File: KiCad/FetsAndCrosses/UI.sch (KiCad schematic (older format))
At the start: 0 parts

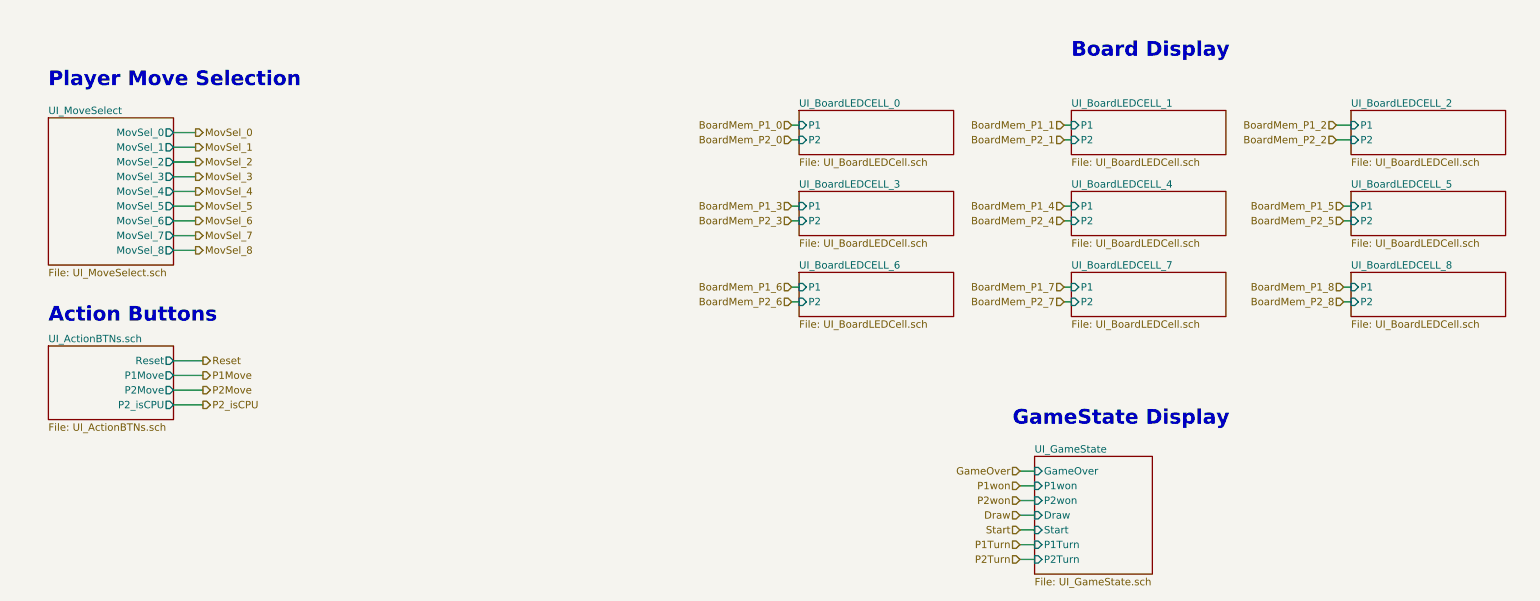
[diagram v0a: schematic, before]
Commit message: Reworked everything to use Buses
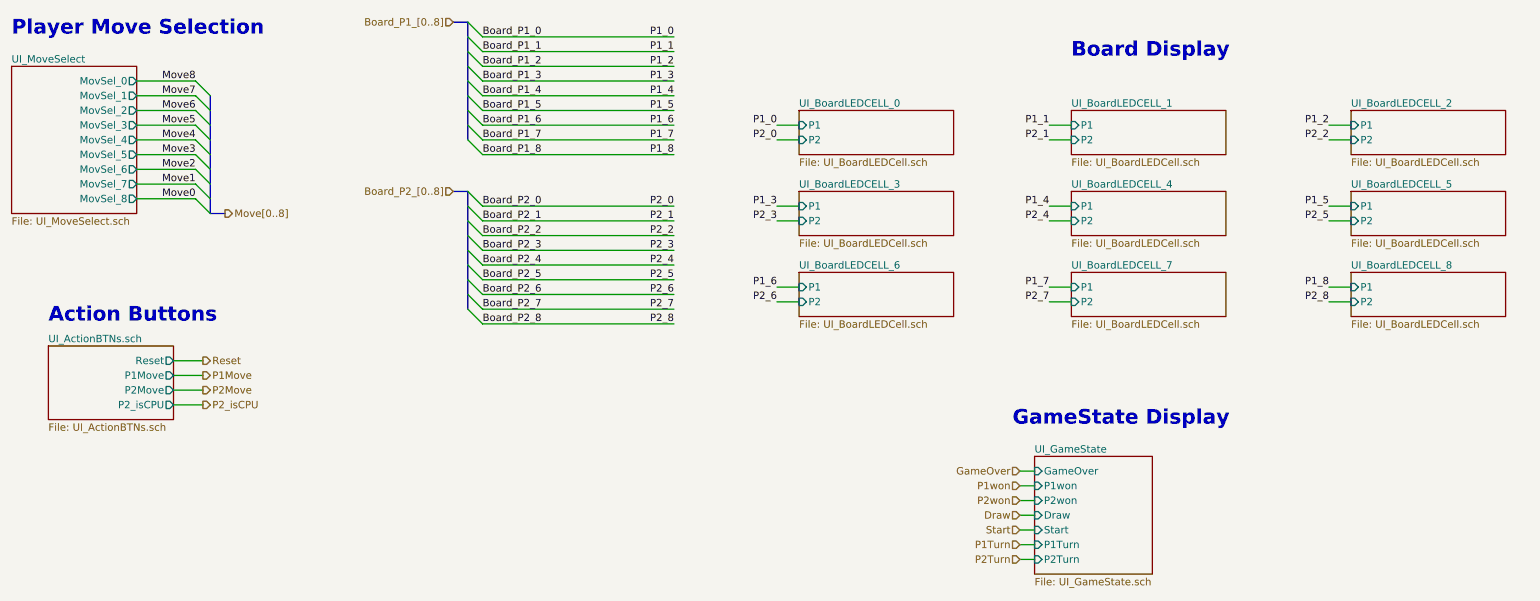
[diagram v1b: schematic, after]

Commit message: Schematic Done, Footprints assigned, ERC OK.
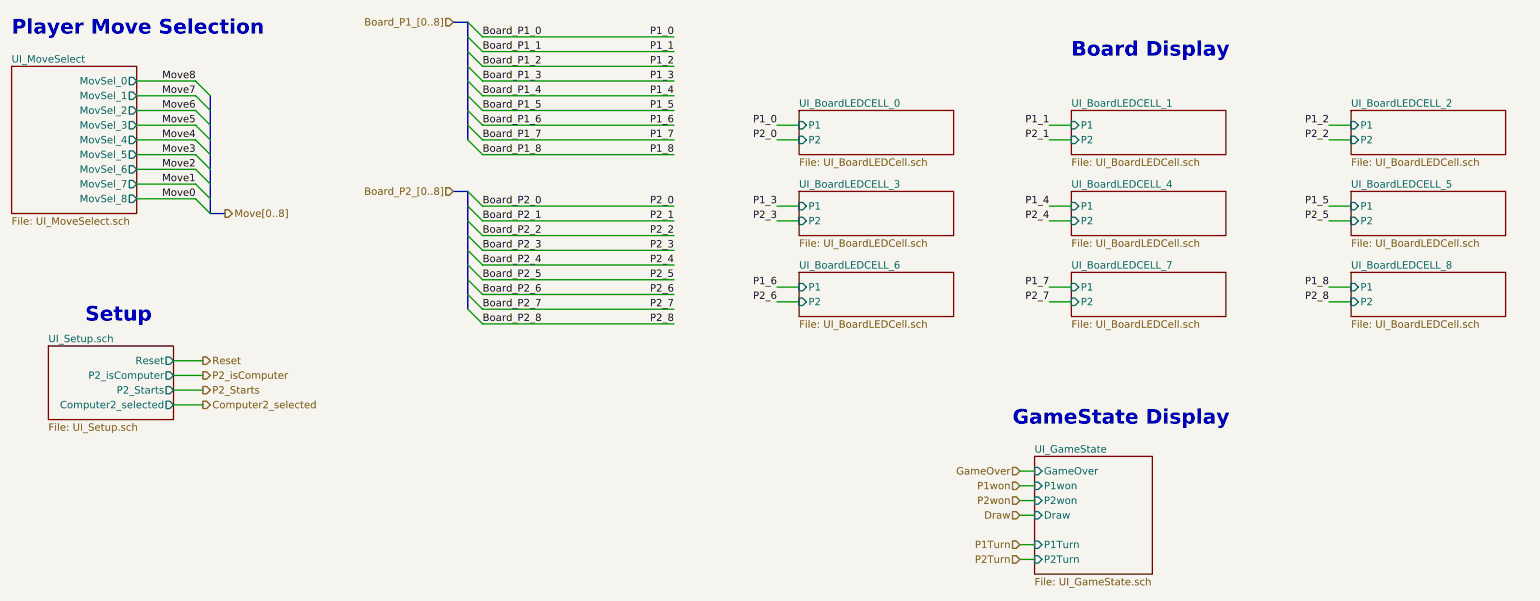
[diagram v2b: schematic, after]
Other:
- note added: "Setup"
- note removed: "Action Buttons"
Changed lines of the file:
@@
 $Descr A4 11693 8268
 encoding utf-8
-Sheet 373 400
+Sheet 373 389
 Title "Fets and Crosses"
 Date ""
@@
 F3 "P2" I L 9800 2850 50
 $EndSheet
-Text Notes 7900 1200 0    100  ~ 20
-Board Display
-Text Notes 700  1050 0    100  ~ 20
-Player Move Selection
 $Sheet
 S 700  1250 850  1000
@@
 F10 "MovSel_7" O R 1550 2050 50
 $EndSheet
-Text Notes 950  3000 0    100  ~ 20
-Action Buttons
 $Sheet
 S 950  3150 850  500
 U 5E6A228F
-F0 "UI_ActionBTNs.sch" 50
-F1 "UI_ActionBTNs.sch" 50
+F0 "UI_Setup.sch" 50
+F1 "UI_Setup.sch" 50
 F2 "Reset" O R 1800 3250 50
-F3 "P1Move" O R 1800 3350 50
-F4 "P2Move" O R 1800 3450 50
-F5 "P2_isCPU" O R 1800 3550 50
-$EndSheet
-Text HLabel 2000 3250 2    50   Output ~ 0
-Reset
-Text HLabel 2000 3350 2    50   Output ~ 0
-P1Move
-Text HLabel 2000 3450 2    50   Output ~ 0
-P2Move
-Text HLabel 2000 3550 2    50   Output ~ 0
-P2_isCPU
-Wire Wire Line
-	2000 3250 1800 3250
-Wire Wire Line
-	2000 3350 1800 3350
-Wire Wire Line
-	2000 3450 1800 3450
-Wire Wire Line
-	2000 3550 1800 3550
-Text Notes 7500 3700 0    100  ~ 20
-GameState Display
+F3 "P2_isComputer" O R 1800 3350 50
+F4 "P2_Starts" O R 1800 3450 50
+F5 "Computer2_selected" O R 1800 3550 50
+$EndSheet
 $Sheet
 S 7650 3900 800  800
@@
 F4 "P2won" I L 7650 4200 50
 F5 "Draw" I L 7650 4300 50
-F6 "Start" I L 7650 4400 50
-F7 "P1Turn" I L 7650 4500 50
-F8 "P2Turn" I L 7650 4600 50
-$EndSheet
+F6 "P1Turn" I L 7650 4500 50
+F7 "P2Turn" I L 7650 4600 50
+$EndSheet
+Text Notes 7900 1200 0    100  ~ 20
+Board Display
+Text Notes 700  1050 0    100  ~ 20
+Player Move Selection
+Text Notes 1200 3000 0    100  ~ 20
+Setup
+Text HLabel 2000 3250 2    50   Output ~ 0
+Reset
+Text HLabel 2000 3350 2    50   Output ~ 0
+P2_isComputer
+Text Notes 7500 3700 0    100  ~ 20
+GameState Display
 Text HLabel 7550 4000 0    50   Input ~ 0
 GameOver
@@
 Text HLabel 7550 4300 0    50   Input ~ 0
 Draw
-Text HLabel 7550 4400 0    50   Input ~ 0
-Start
 Text HLabel 7550 4500 0    50   Input ~ 0
 P1Turn
 Text HLabel 7550 4600 0    50   Input ~ 0
 P2Turn
-Wire Wire Line
-	7550 4000 7650 4000
-Wire Wire Line
-	7550 4100 7650 4100
-Wire Wire Line
-	7550 4200 7650 4200
-Wire Wire Line
-	7550 4300 7650 4300
-Wire Wire Line
-	7550 4400 7650 4400
-Wire Wire Line
-	7550 4500 7650 4500
-Wire Wire Line
-	7550 4600 7650 4600
-Entry Wire Line
-	3800 1750 3900 1850
-Entry Wire Line
-	3800 1650 3900 1750
-Entry Wire Line
-	3800 1550 3900 1650
-Entry Wire Line
-	3800 1450 3900 1550
-Entry Wire Line
-	3800 1350 3900 1450
-Entry Wire Line
-	3800 1250 3900 1350
-Entry Wire Line
-	3800 1150 3900 1250
-Entry Wire Line
-	3800 1050 3900 1150
-Entry Wire Line
-	3800 950  3900 1050
-Wire Bus Line
-	3700 950  3800 950
 Text HLabel 3700 950  0    50   Input ~ 0
 Board_P1_[0..8]
-Wire Wire Line
-	3900 1050 5200 1050
-Wire Wire Line
-	3900 1150 5200 1150
-Wire Wire Line
-	3900 1250 5200 1250
-Wire Wire Line
-	3900 1350 5200 1350
-Wire Wire Line
-	3900 1450 5200 1450
-Wire Wire Line
-	3900 1550 5200 1550
-Wire Wire Line
-	3900 1650 5200 1650
-Wire Wire Line
-	3900 1750 5200 1750
-Wire Wire Line
-	3900 1850 5200 1850
-Entry Wire Line
-	3800 2900 3900 3000
-Entry Wire Line
-	3800 2800 3900 2900
-Entry Wire Line
-	3800 2700 3900 2800
-Entry Wire Line
-	3800 2600 3900 2700
-Entry Wire Line
-	3800 2500 3900 2600
-Entry Wire Line
-	3800 2400 3900 2500
-Entry Wire Line
-	3800 2300 3900 2400
-Entry Wire Line
-	3800 2200 3900 2300
-Entry Wire Line
-	3800 2100 3900 2200
-Wire Bus Line
-	3700 2100 3800 2100
 Text HLabel 3700 2100 0    50   Input ~ 0
 Board_P2_[0..8]
-Wire Wire Line
-	3900 2200 5200 2200
-Wire Wire Line
-	3900 2300 5200 2300
-Wire Wire Line
-	3900 2400 5200 2400
-Wire Wire Line
-	3900 2500 5200 2500
-Wire Wire Line
-	3900 2600 5200 2600
-Wire Wire Line
-	3900 2700 5200 2700
-Wire Wire Line
-	3900 2800 5200 2800
-Wire Wire Line
-	3900 2900 5200 2900
-Wire Wire Line
-	3900 3000 5200 3000
 Text Label 3900 1050 0    50   ~ 0
 Board_P1_0
@@
 Text Label 3900 3000 0    50   ~ 0
 Board_P2_8
-Wire Wire Line
-	5900 1650 6050 1650
-Wire Wire Line
-	5900 1750 6050 1750
-Wire Wire Line
-	5900 2300 6050 2300
-Wire Wire Line
-	5900 2200 6050 2200
-Wire Wire Line
-	5900 2850 6050 2850
-Wire Wire Line
-	5900 2750 6050 2750
-Wire Wire Line
-	7750 1650 7900 1650
-Wire Wire Line
-	7750 1750 7900 1750
-Wire Wire Line
-	7750 2300 7900 2300
-Wire Wire Line
-	7750 2200 7900 2200
-Wire Wire Line
-	7750 2850 7900 2850
-Wire Wire Line
-	7750 2750 7900 2750
-Wire Wire Line
-	9650 1650 9800 1650
-Wire Wire Line
-	9650 1750 9800 1750
-Wire Wire Line
-	9650 2300 9800 2300
-Wire Wire Line
-	9650 2200 9800 2200
-Wire Wire Line
-	9650 2750 9800 2750
-Wire Wire Line
-	9650 2850 9800 2850
 Text Label 5200 1050 2    50   ~ 0
 P1_0
@@
 Text Label 9650 2850 2    50   ~ 0
 P2_8
-Entry Wire Line
-	2050 2250 1950 2150
-Entry Wire Line
-	2050 2150 1950 2050
-Entry Wire Line
-	2050 2050 1950 1950
-Entry Wire Line
-	2050 1950 1950 1850
-Entry Wire Line
-	2050 1850 1950 1750
-Entry Wire Line
-	2050 1750 1950 1650
-Entry Wire Line
-	2050 1650 1950 1550
-Entry Wire Line
-	2050 1550 1950 1450
-Entry Wire Line
-	2050 1450 1950 1350
-Wire Bus Line
-	2050 2250 2150 2250
 Text HLabel 2150 2250 2    50   Output ~ 0
 Move[0..8]
@@
 Text Label 1950 1350 2    50   ~ 0
 Move8
+Text HLabel 2000 3450 2    50   Output ~ 0
+P2_Starts
+Text HLabel 2000 3550 2    50   Output ~ 0
+Computer2_selected
+Wire Wire Line
+	2000 3250 1800 3250
+Wire Wire Line
+	2000 3450 1800 3450
+Wire Wire Line
+	7550 4000 7650 4000
+Wire Wire Line
+	7550 4100 7650 4100
+Wire Wire Line
+	7550 4200 7650 4200
+Wire Wire Line
+	7550 4300 7650 4300
+Wire Wire Line
+	7550 4500 7650 4500
+Wire Wire Line
+	7550 4600 7650 4600
+Wire Bus Line
+	3700 950  3800 950
+Wire Wire Line
+	3900 1050 5200 1050
+Wire Wire Line
+	3900 1150 5200 1150
+Wire Wire Line
+	3900 1250 5200 1250
+Wire Wire Line
+	3900 1350 5200 1350
+Wire Wire Line
+	3900 1450 5200 1450
+Wire Wire Line
+	3900 1550 5200 1550
+Wire Wire Line
+	3900 1650 5200 1650
+Wire Wire Line
+	3900 1750 5200 1750
+Wire Wire Line
+	3900 1850 5200 1850
+Wire Bus Line
+	3700 2100 3800 2100
+Wire Wire Line
+	3900 2200 5200 2200
+Wire Wire Line
+	3900 2300 5200 2300
+Wire Wire Line
+	3900 2400 5200 2400
+Wire Wire Line
+	3900 2500 5200 2500
+Wire Wire Line
+	3900 2600 5200 2600
+Wire Wire Line
+	3900 2700 5200 2700
+Wire Wire Line
+	3900 2800 5200 2800
+Wire Wire Line
+	3900 2900 5200 2900
+Wire Wire Line
+	3900 3000 5200 3000
+Wire Wire Line
+	5900 1650 6050 1650
+Wire Wire Line
+	5900 1750 6050 1750
+Wire Wire Line
+	5900 2300 6050 2300
+Wire Wire Line
+	5900 2200 6050 2200
+Wire Wire Line
+	5900 2850 6050 2850
+Wire Wire Line
+	5900 2750 6050 2750
+Wire Wire Line
+	7750 1650 7900 1650
+Wire Wire Line
+	7750 1750 7900 1750
+Wire Wire Line
+	7750 2300 7900 2300
+Wire Wire Line
+	7750 2200 7900 2200
+Wire Wire Line
+	7750 2850 7900 2850
+Wire Wire Line
+	7750 2750 7900 2750
+Wire Wire Line
+	9650 1650 9800 1650
+Wire Wire Line
+	9650 1750 9800 1750
+Wire Wire Line
+	9650 2300 9800 2300
+Wire Wire Line
+	9650 2200 9800 2200
+Wire Wire Line
+	9650 2750 9800 2750
+Wire Wire Line
+	9650 2850 9800 2850
+Wire Bus Line
+	2050 2250 2150 2250
 Wire Wire Line
 	1550 1350 1950 1350
@@
 Wire Wire Line
 	1550 2150 1950 2150
+Wire Wire Line
+	2000 3350 1800 3350
+Wire Wire Line
+	1800 3550 2000 3550
+Entry Wire Line
+	3800 1750 3900 1850
+Entry Wire Line
+	3800 1650 3900 1750
+Entry Wire Line
+	3800 1550 3900 1650
+Entry Wire Line
+	3800 1450 3900 1550
+Entry Wire Line
+	3800 1350 3900 1450
+Entry Wire Line
+	3800 1250 3900 1350
+Entry Wire Line
+	3800 1150 3900 1250
+Entry Wire Line
+	3800 1050 3900 1150
+Entry Wire Line
+	3800 950  3900 1050
+Entry Wire Line
+	3800 2900 3900 3000
+Entry Wire Line
+	3800 2800 3900 2900
+Entry Wire Line
+	3800 2700 3900 2800
+Entry Wire Line
+	3800 2600 3900 2700
+Entry Wire Line
+	3800 2500 3900 2600
+Entry Wire Line
+	3800 2400 3900 2500
+Entry Wire Line
+	3800 2300 3900 2400
+Entry Wire Line
+	3800 2200 3900 2300
+Entry Wire Line
+	3800 2100 3900 2200
+Entry Wire Line
+	2050 2250 1950 2150
+Entry Wire Line
+	2050 2150 1950 2050
+Entry Wire Line
+	2050 2050 1950 1950
+Entry Wire Line
+	2050 1950 1950 1850
+Entry Wire Line
+	2050 1850 1950 1750
+Entry Wire Line
+	2050 1750 1950 1650
+Entry Wire Line
+	2050 1650 1950 1550
+Entry Wire Line
+	2050 1550 1950 1450
+Entry Wire Line
+	2050 1450 1950 1350
 Wire Bus Line
 	3800 2100 3800 2900

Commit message: PCB v1.0 layout mostly done.
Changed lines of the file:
@@
 $Descr A4 11693 8268
 encoding utf-8
-Sheet 344 362
+Sheet 346 362
 Title "Fets and Crosses"
 Date "2020-09-15"
@@
 $EndSheet
 $Sheet
-S 950  3150 850  500
+S 950  3150 850  400
 U 5E6A228F
 F0 "UI_Setup.sch" 50
@@
 F3 "P2_isComputer" O R 1800 3350 50
 F4 "P2_Starts" O R 1800 3450 50
-F5 "Computer2_selected" O R 1800 3550 50
 $EndSheet
 $Sheet
@@
 Text HLabel 2000 3450 2    50   Output ~ 0
 P2_Starts
-Text HLabel 2000 3550 2    50   Output ~ 0
-Computer2_selected
 Wire Wire Line
 	2000 3250 1800 3250
@@
 Wire Wire Line
 	2000 3350 1800 3350
-Wire Wire Line
-	1800 3550 2000 3550
 Entry Wire Line
 	3800 1750 3900 1850
